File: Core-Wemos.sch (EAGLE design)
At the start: 49 parts, among them CON1 0.100, J2 2mm, J3 IO4, Q1 BSS138, Q2 BSS138, Q3 BSS138, Q4 BSS138, Q5 BSS138, Q6 BSS138, Q7 BSS138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

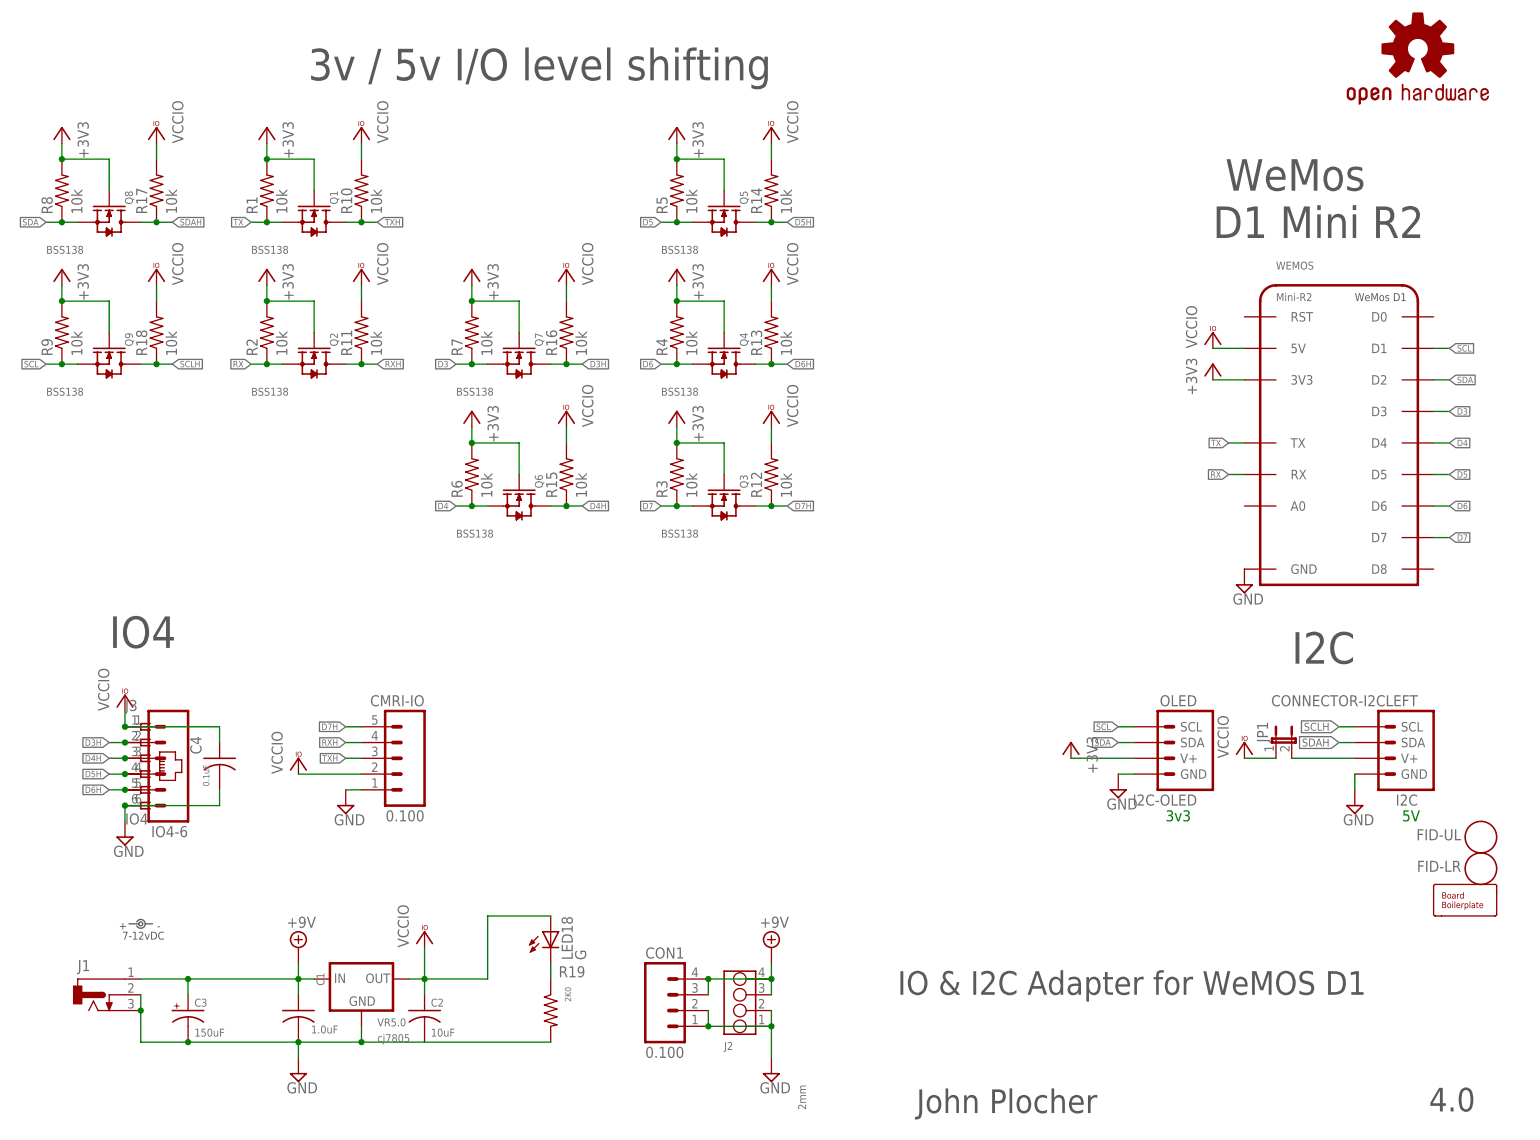
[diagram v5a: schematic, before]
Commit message: updated part names
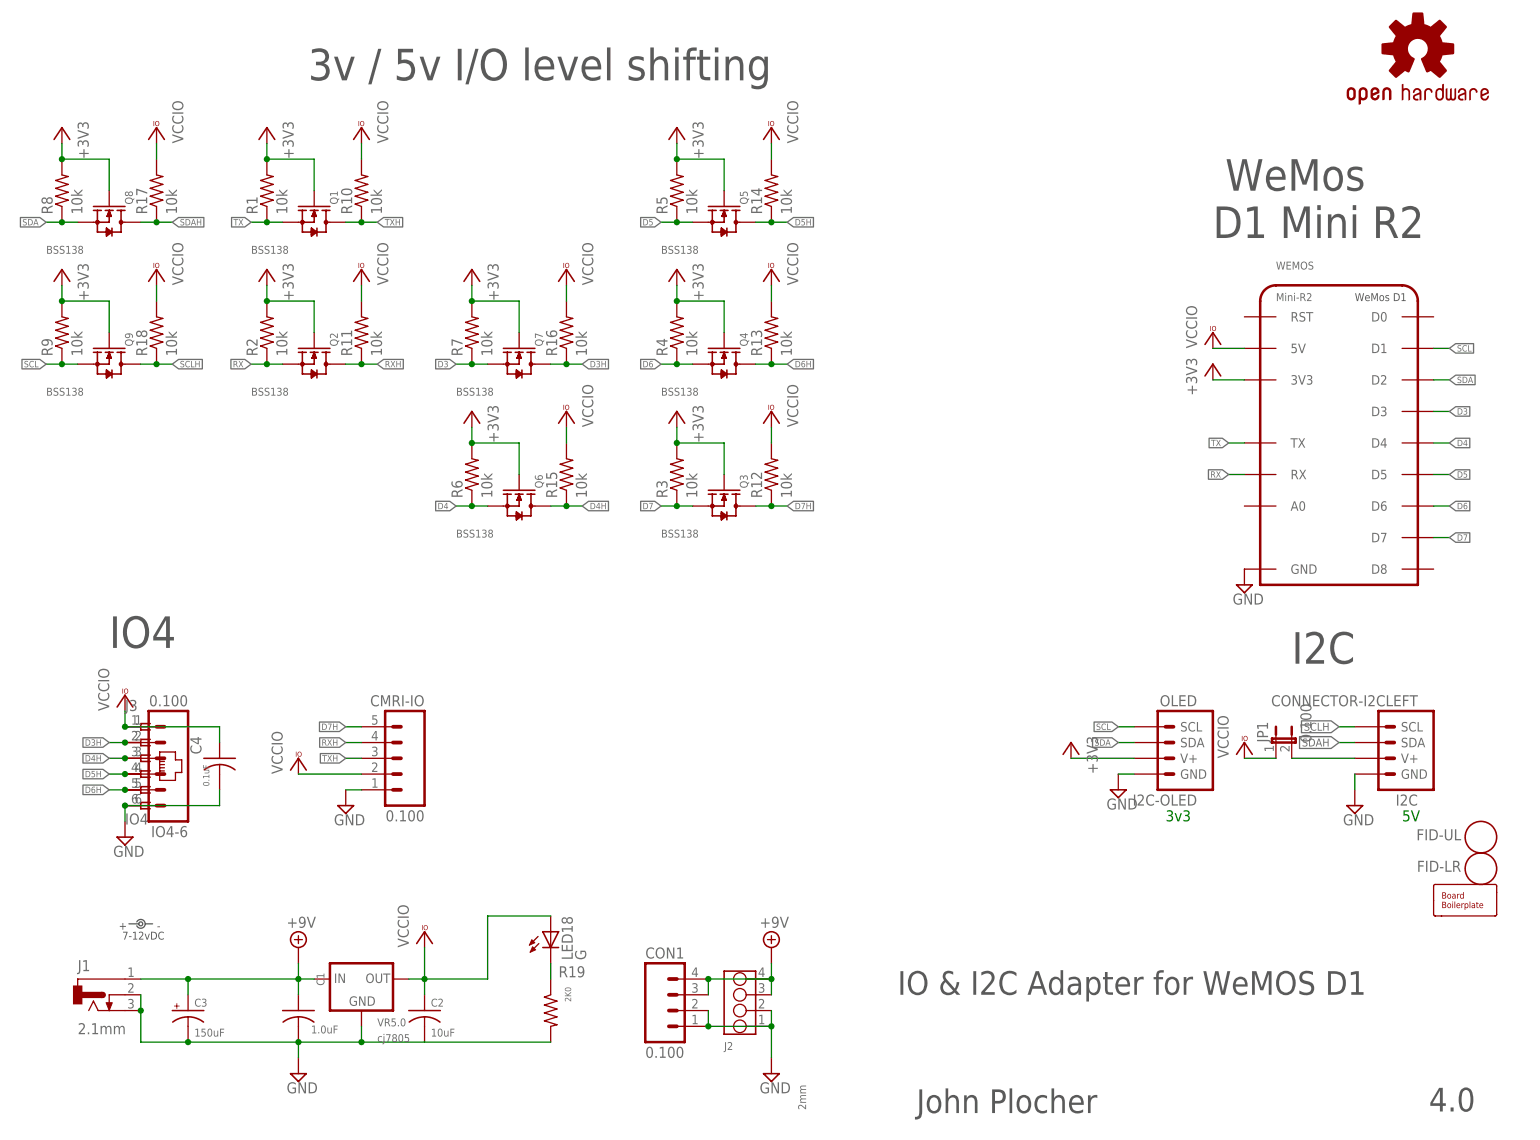
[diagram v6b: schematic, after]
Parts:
- BOARD: value BOARD80X150 -> BOARD80X80
- IO4-6, JP1: value (none) -> 0.100
- J1: value (none) -> 2.1mm
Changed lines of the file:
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@@
 <part name="VCC4" library="supply1" deviceset="VCCIO" device=""/>
 <part name="J3" library="SPCoast" deviceset="CONNECTOR-RJ25" device="-6P6C" value="IO4"/>
-<part name="IO4-6" library="SPCoast" deviceset="CONNECTOR-M06" device="LOCK"/>
+<part name="IO4-6" library="SPCoast" deviceset="CONNECTOR-M06" device="LOCK" value="0.100"/>
 <part name="I2C" library="SPCoast" deviceset="CONNECTOR-I2C" device="LEFT" value="CONNECTOR-I2CLEFT"/>
 <part name="V1" library="supply2" deviceset="GND" device=""/>
@@
 <part name="V5" library="supply2" deviceset="GND" device=""/>
 <part name="SUPPLY1" library="supply2" deviceset="+9V" device=""/>
-<part name="J1" library="SPCoast" deviceset="CONNECTOR-DC-POWER" device="-RA"/>
+<part name="J1" library="SPCoast" deviceset="CONNECTOR-DC-POWER" device="-RA" value="2.1mm"/>
 <part name="LABEL1" library="SPCoast" deviceset="DOC-POWER_LABEL" device="" value="7-12vDC"/>
 <part name="VCC12" library="supply1" deviceset="VCCIO" device=""/>
-<part name="BOARD" library="SPCoast" deviceset="BOARD" device="80X80-NOHOLES" value="BOARD80X150"/>
+<part name="BOARD" library="SPCoast" deviceset="BOARD" device="80X80-NOHOLES" value="BOARD80X80"/>
 <part name="C2" library="SPCoast" deviceset="CAP*" device="0805" value="10uF"/>
 <part name="C1" library="SPCoast" deviceset="CAP*" device="0805" value="1.0uF"/>
@@
 <part name="LED18" library="SPCoast" deviceset="LED*" device="0603-LED" value="G"/>
 <part name="CON1" library="SPCoast" deviceset="CONNECTOR-M04" device="LOCK" value="0.100"/>
-<part name="JP1" library="SPCoast" deviceset="JUMPER-2" device="PTH_LOCK"/>
+<part name="JP1" library="SPCoast" deviceset="JUMPER-2" device="PTH_LOCK" value="0.100"/>
 </parts>
 <sheets>

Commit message: normalized values
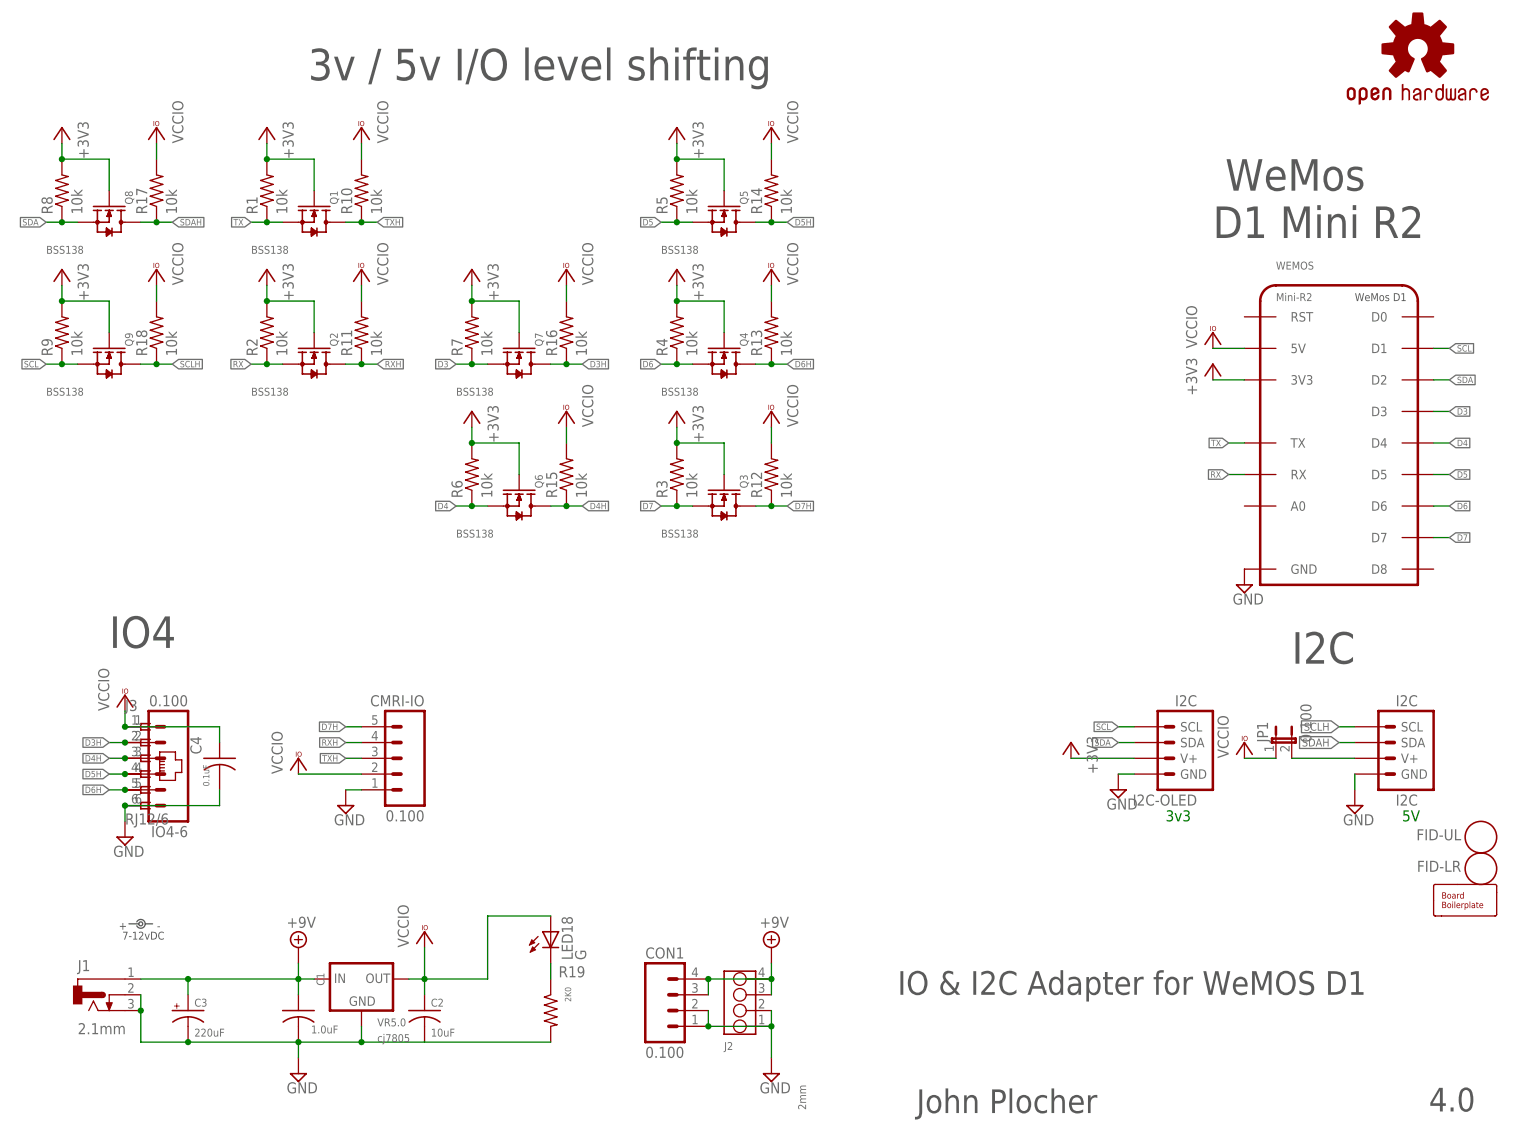
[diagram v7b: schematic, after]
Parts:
- BOARD: value BOARD80X80 -> BOARD
- C1, C2, C4: device SPCoast:CAP0805 -> SPCoast:CAP0603
- C3: value 150uF -> 220uF
- I2C: value CONNECTOR-I2CLEFT -> I2C
- I2C-OLED: value OLED -> I2C
- J3: value IO4 -> RJ12/6
- OSHW1: value OSHW-LOGOL -> OSHW
- R1, R10, R11, R12, R13, R14, R15, R16, R17, R18, R2, R3, R4, R5, R6, R7, R8, R9: device SPCoast:R0805-RES -> SPCoast:R0603-RES
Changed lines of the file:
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@@
 <parts>
 <part name="FRAME1" library="MCP" deviceset="FRAME-LETTER" device=""/>
-<part name="OSHW1" library="SparkFun" deviceset="OSHW-LOGO" device="L" value="OSHW-LOGOL"/>
+<part name="OSHW1" library="SparkFun" deviceset="OSHW-LOGO" device="L" value="OSHW"/>
 <part name="V3" library="supply2" deviceset="GND" device=""/>
 <part name="SUPPLY2" library="supply2" deviceset="+9V" device=""/>
 <part name="V12" library="supply2" deviceset="GND" device=""/>
 <part name="VCC4" library="supply1" deviceset="VCCIO" device=""/>
-<part name="J3" library="SPCoast" deviceset="CONNECTOR-RJ25" device="-6P6C" value="IO4"/>
+<part name="J3" library="SPCoast" deviceset="CONNECTOR-RJ25" device="-6P6C" value="RJ12/6"/>
 <part name="IO4-6" library="SPCoast" deviceset="CONNECTOR-M06" device="LOCK" value="0.100"/>
-<part name="I2C" library="SPCoast" deviceset="CONNECTOR-I2C" device="LEFT" value="CONNECTOR-I2CLEFT"/>
+<part name="I2C" library="SPCoast" deviceset="CONNECTOR-I2C" device="LEFT" value="I2C"/>
 <part name="V1" library="supply2" deviceset="GND" device=""/>
 <part name="J2" library="SPCoast" deviceset="CONNECTOR-GROVE-4P-2.0" device="-3470130P1" value="2mm"/>
@@
 <part name="LABEL1" library="SPCoast" deviceset="DOC-POWER_LABEL" device="" value="7-12vDC"/>
 <part name="VCC12" library="supply1" deviceset="VCCIO" device=""/>
-<part name="BOARD" library="SPCoast" deviceset="BOARD" device="80X80-NOHOLES" value="BOARD80X80"/>
-<part name="C2" library="SPCoast" deviceset="CAP*" device="0805" value="10uF"/>
-<part name="C1" library="SPCoast" deviceset="CAP*" device="0805" value="1.0uF"/>
+<part name="BOARD" library="SPCoast" deviceset="BOARD" device="80X80-NOHOLES" value="BOARD"/>
+<part name="C2" library="SPCoast" deviceset="CAP*" device="0603" value="10uF"/>
+<part name="C1" library="SPCoast" deviceset="CAP*" device="0603" value="1.0uF"/>
 <part name="VR5.0" library="SPCoast" deviceset="VREG-?-*" device="DPAK" technology="5" value="cj7805"/>
-<part name="C4" library="SPCoast" deviceset="CAP*" device="0805" value="0.1uF"/>
+<part name="C4" library="SPCoast" deviceset="CAP*" device="0603" value="0.1uF"/>
 <part name="WEMOS" library="SPCoast" deviceset="WEMOS-D1" device="V1" value="Mini-R2"/>
 <part name="V7" library="supply2" deviceset="GND" device=""/>
@@
 <part name="VCC24" library="supply1" deviceset="VCCIO" device=""/>
 <part name="VCC8" library="supply1" deviceset="VCCIO" device=""/>
-<part name="C3" library="SPCoast" deviceset="CAP-POL*" device="0810" value="150uF"/>
+<part name="C3" library="SPCoast" deviceset="CAP-POL*" device="0810" value="220uF"/>
 <part name="Q7" library="SPCoast" deviceset="MOSFET-N-*-?" device="SOT23" technology="BSS138" value="BSS138"/>
-<part name="R7" library="SPCoast" deviceset="R*" device="0805-RES" value="10k"/>
-<part name="R16" library="SPCoast" deviceset="R*" device="0805-RES" value="10k"/>
+<part name="R7" library="SPCoast" deviceset="R*" device="0603-RES" value="10k"/>
+<part name="R16" library="SPCoast" deviceset="R*" device="0603-RES" value="10k"/>
 <part name="3V4" library="supply1" deviceset="+3V3" device=""/>
 <part name="VCC3" library="supply1" deviceset="VCCIO" device=""/>
 <part name="Q8" library="SPCoast" deviceset="MOSFET-N-*-?" device="SOT23" technology="BSS138" value="BSS138"/>
-<part name="R8" library="SPCoast" deviceset="R*" device="0805-RES" value="10k"/>
-<part name="R17" library="SPCoast" deviceset="R*" device="0805-RES" value="10k"/>
+<part name="R8" library="SPCoast" deviceset="R*" device="0603-RES" value="10k"/>
+<part name="R17" library="SPCoast" deviceset="R*" device="0603-RES" value="10k"/>
 <part name="3V3" library="supply1" deviceset="+3V3" device=""/>
 <part name="VCC5" library="supply1" deviceset="VCCIO" device=""/>
 <part name="Q9" library="SPCoast" deviceset="MOSFET-N-*-?" device="SOT23" technology="BSS138" value="BSS138"/>
-<part name="R9" library="SPCoast" deviceset="R*" device="0805-RES" value="10k"/>
-<part name="R18" library="SPCoast" deviceset="R*" device="0805-RES" value="10k"/>
+<part name="R9" library="SPCoast" deviceset="R*" device="0603-RES" value="10k"/>
+<part name="R18" library="SPCoast" deviceset="R*" device="0603-RES" value="10k"/>
 <part name="3V5" library="supply1" deviceset="+3V3" device=""/>
 <part name="VCC7" library="supply1" deviceset="VCCIO" device=""/>
 <part name="Q1" library="SPCoast" deviceset="MOSFET-N-*-?" device="SOT23" technology="BSS138" value="BSS138"/>
-<part name="R1" library="SPCoast" deviceset="R*" device="0805-RES" value="10k"/>
-<part name="R10" library="SPCoast" deviceset="R*" device="0805-RES" value="10k"/>
+<part name="R1" library="SPCoast" deviceset="R*" device="0603-RES" value="10k"/>
+<part name="R10" library="SPCoast" deviceset="R*" device="0603-RES" value="10k"/>
 <part name="3V1" library="supply1" deviceset="+3V3" device=""/>
 <part name="VCC1" library="supply1" deviceset="VCCIO" device=""/>
 <part name="Q2" library="SPCoast" deviceset="MOSFET-N-*-?" device="SOT23" technology="BSS138" value="BSS138"/>
-<part name="R2" library="SPCoast" deviceset="R*" device="0805-RES" value="10k"/>
-<part name="R11" library="SPCoast" deviceset="R*" device="0805-RES" value="10k"/>
+<part name="R2" library="SPCoast" deviceset="R*" device="0603-RES" value="10k"/>
+<part name="R11" library="SPCoast" deviceset="R*" device="0603-RES" value="10k"/>
 <part name="3V6" library="supply1" deviceset="+3V3" device=""/>
 <part name="VCC9" library="supply1" deviceset="VCCIO" device=""/>
 <part name="Q3" library="SPCoast" deviceset="MOSFET-N-*-?" device="SOT23" technology="BSS138" value="BSS138"/>
-<part name="R3" library="SPCoast" deviceset="R*" device="0805-RES" value="10k"/>
-<part name="R12" library="SPCoast" deviceset="R*" device="0805-RES" value="10k"/>
+<part name="R3" library="SPCoast" deviceset="R*" device="0603-RES" value="10k"/>
+<part name="R12" library="SPCoast" deviceset="R*" device="0603-RES" value="10k"/>
 <part name="3V7" library="supply1" deviceset="+3V3" device=""/>
 <part name="VCC10" library="supply1" deviceset="VCCIO" device=""/>
 <part name="Q4" library="SPCoast" deviceset="MOSFET-N-*-?" device="SOT23" technology="BSS138" value="BSS138"/>
-<part name="R4" library="SPCoast" deviceset="R*" device="0805-RES" value="10k"/>
-<part name="R13" library="SPCoast" deviceset="R*" device="0805-RES" value="10k"/>
+<part name="R4" library="SPCoast" deviceset="R*" device="0603-RES" value="10k"/>
+<part name="R13" library="SPCoast" deviceset="R*" device="0603-RES" value="10k"/>
 <part name="3V2" library="supply1" deviceset="+3V3" device=""/>
 <part name="VCC6" library="supply1" deviceset="VCCIO" device=""/>
 <part name="Q5" library="SPCoast" deviceset="MOSFET-N-*-?" device="SOT23" technology="BSS138" value="BSS138"/>
-<part name="R5" library="SPCoast" deviceset="R*" device="0805-RES" value="10k"/>
-<part name="R14" library="SPCoast" deviceset="R*" device="0805-RES" value="10k"/>
+<part name="R5" library="SPCoast" deviceset="R*" device="0603-RES" value="10k"/>
+<part name="R14" library="SPCoast" deviceset="R*" device="0603-RES" value="10k"/>
 <part name="3V9" library="supply1" deviceset="+3V3" device=""/>
 <part name="VCC13" library="supply1" deviceset="VCCIO" device=""/>
 <part name="Q6" library="SPCoast" deviceset="MOSFET-N-*-?" device="SOT23" technology="BSS138" value="BSS138"/>
-<part name="R6" library="SPCoast" deviceset="R*" device="0805-RES" value="10k"/>
-<part name="R15" library="SPCoast" deviceset="R*" device="0805-RES" value="10k"/>
+<part name="R6" library="SPCoast" deviceset="R*" device="0603-RES" value="10k"/>
+<part name="R15" library="SPCoast" deviceset="R*" device="0603-RES" value="10k"/>
 <part name="3V10" library="supply1" deviceset="+3V3" device=""/>
 <part name="VCC14" library="supply1" deviceset="VCCIO" device=""/>
@@
 <part name="FID-UL" library="SPCoast" deviceset="FIDUCIAL" device=""/>
 <part name="FID-LR" library="SPCoast" deviceset="FIDUCIAL" device=""/>
-<part name="I2C-OLED" library="SPCoast" deviceset="CONNECTOR-I2C" device="NOOUTLINE" value="OLED"/>
+<part name="I2C-OLED" library="SPCoast" deviceset="CONNECTOR-I2C" device="NOOUTLINE" value="I2C"/>
 <part name="V4" library="supply2" deviceset="GND" device=""/>
 <part name="3V8" library="supply1" deviceset="+3V3" device=""/>
